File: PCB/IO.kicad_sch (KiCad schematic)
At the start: 26 parts, among them J501 Conn_02x03_Counter_Clockwise, J502 USB_C_Receptacle_USB2.0_16P, J503 Screw_Terminal_01x06, J504 Screw_Terminal_01x04, J505 Conn_01x04, J506 Conn_02x03_Counter_Clockwise, J507 Conn_01x05, Q501 NPN

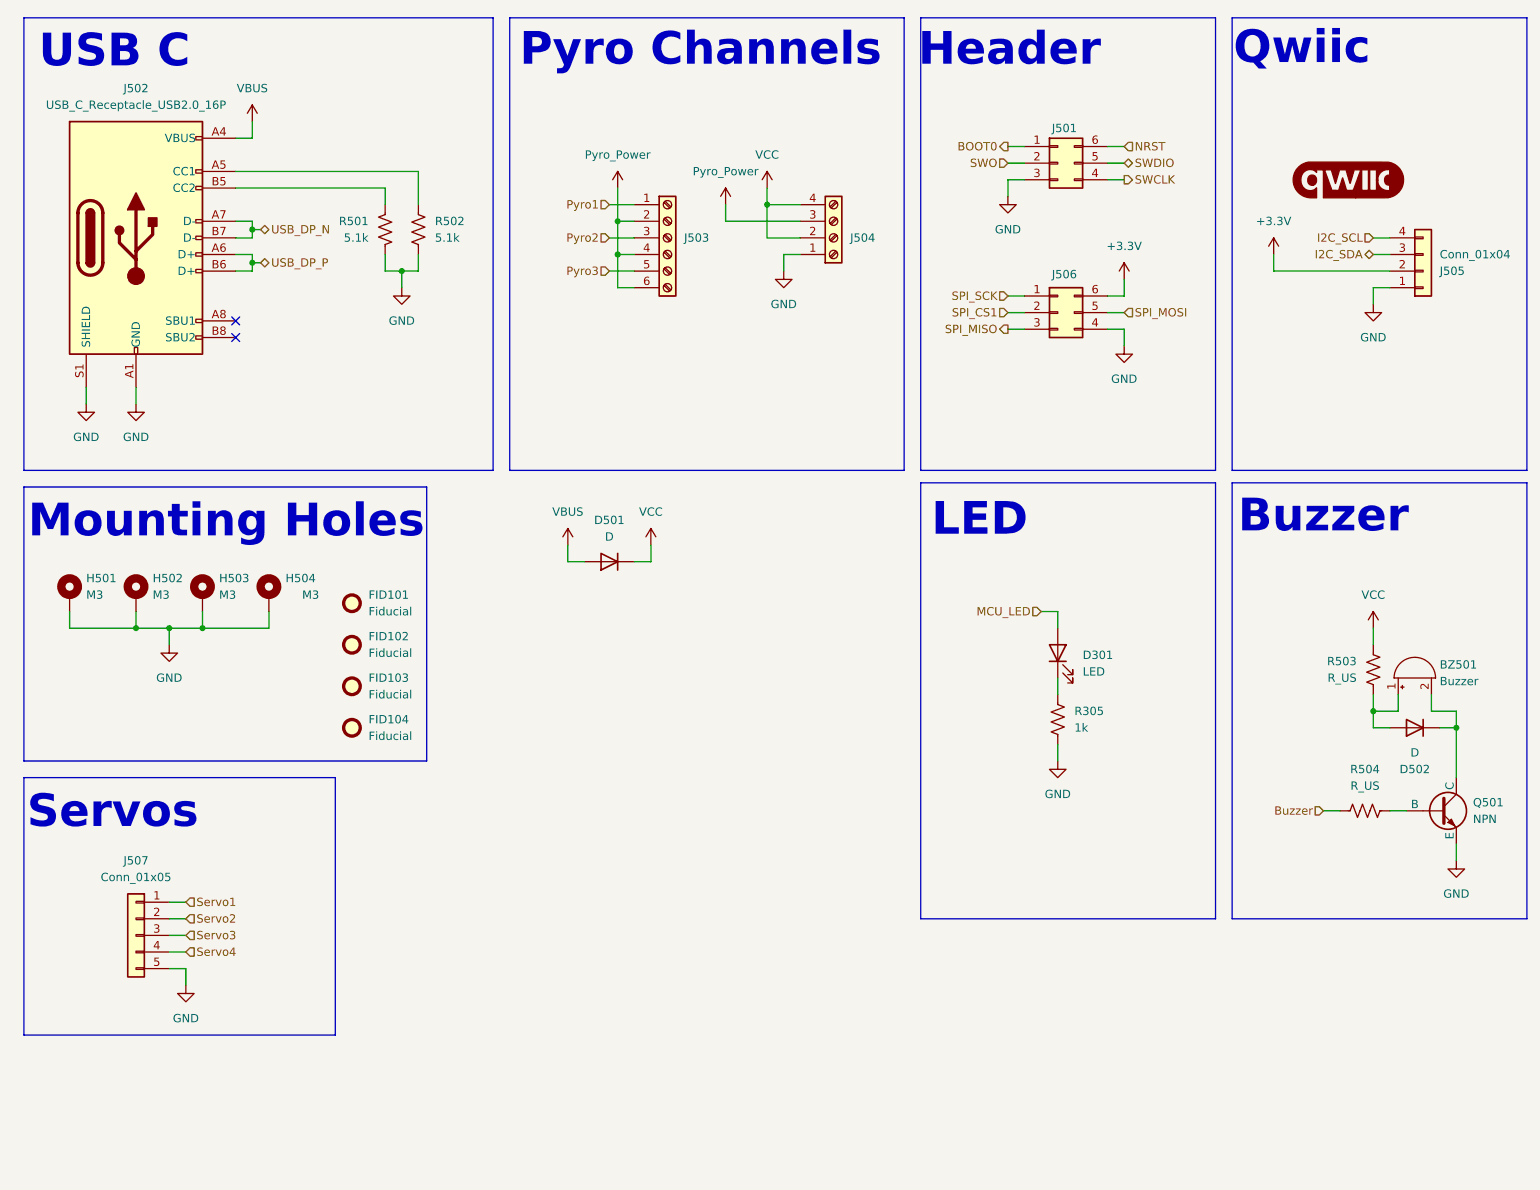
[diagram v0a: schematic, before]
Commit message: Added buzzer Added 2 more leds to MCU Fixed servo connector GND hole shape Added Servo VCC pin Added additional silkscreen for debug connections Added copper plane text "V1.1" Made 915MHz radio trace 50 Ohm
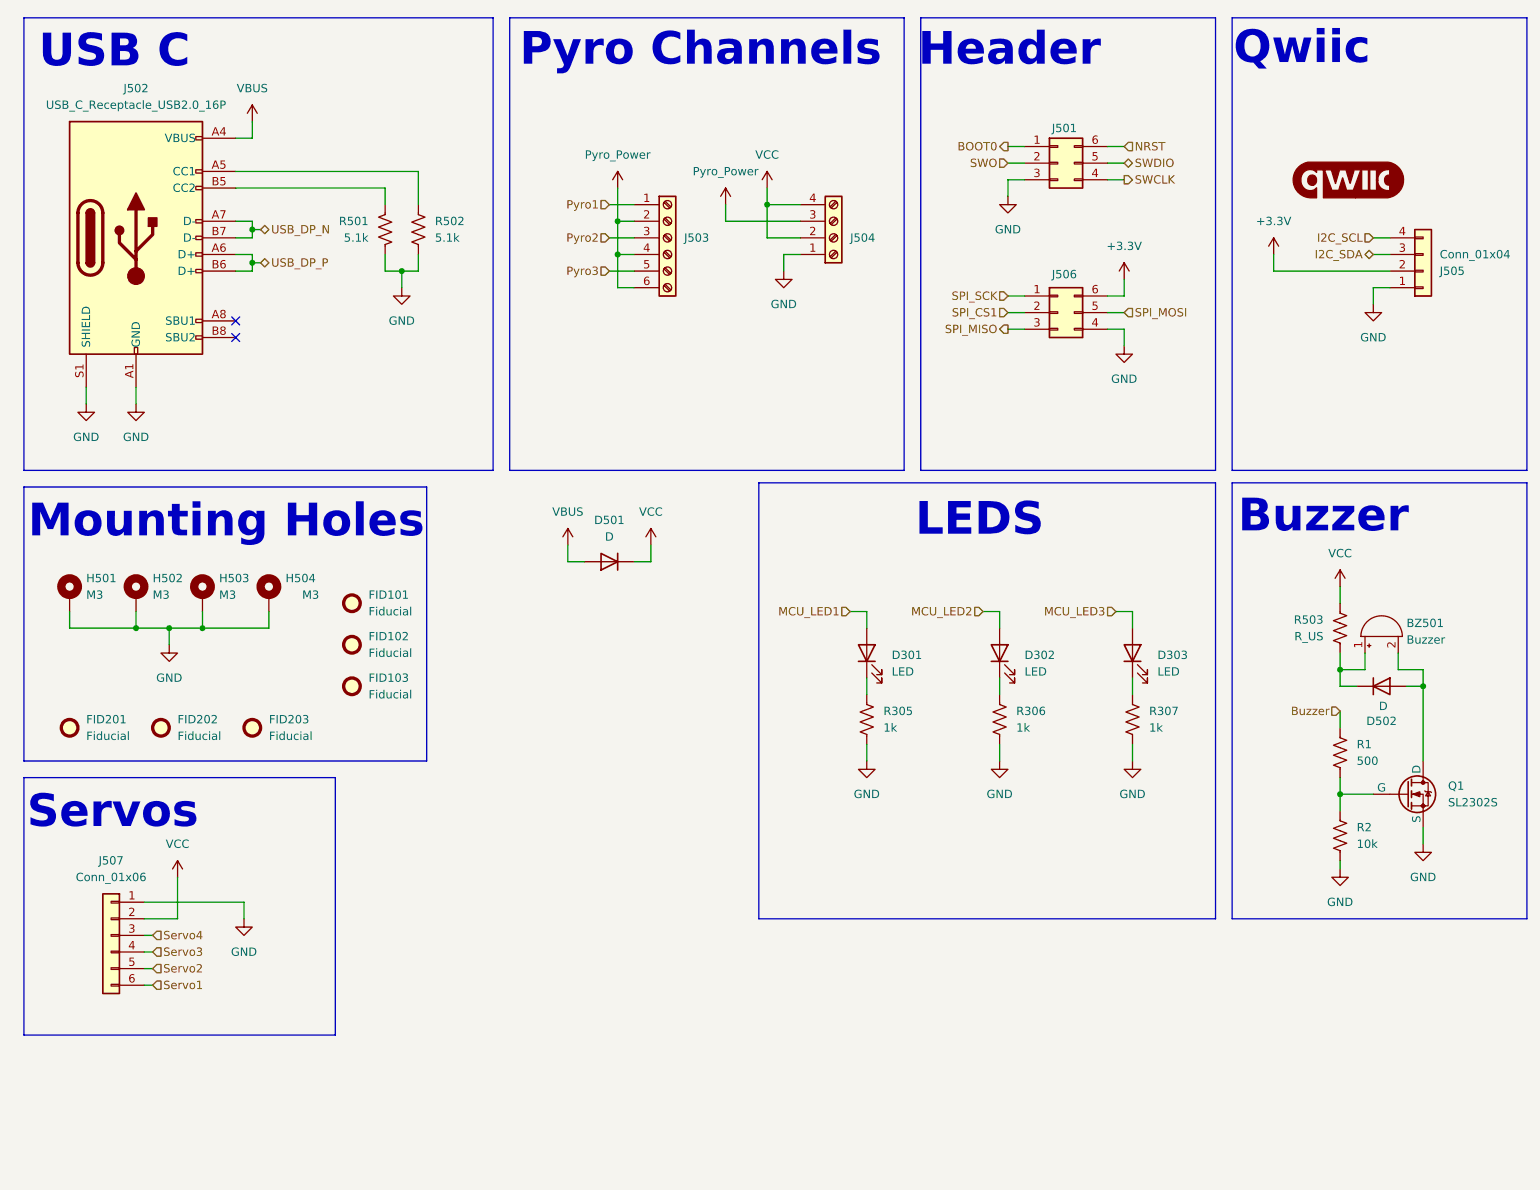
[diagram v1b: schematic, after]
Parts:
- removed Q501: NPN, symbol Simulation_SPICE:NPN
- removed R504: R_US, symbol Device:R_US
- added D301, D303: LED, LED_SMD:LED_0603_1608Metric_Pad1.05x0.95mm_HandSolder, symbol Device:LED
- added FID202, FID203: Fiducial, Fiducial:Fiducial_0.75mm_Mask1.5mm, symbol Mechanical:Fiducial
- added Q1: SL2302S, Package_TO_SOT_SMD:SOT-23-3, symbol Simulation_SPICE:NMOS
- added R1: 500, Resistor_SMD:R_0603_1608Metric_Pad0.98x0.95mm_HandSolder, symbol Device:R_US
- added R2: 10k, Resistor_SMD:R_0603_1608Metric_Pad0.98x0.95mm_HandSolder, symbol Device:R_US
- added R305, R307: 1k, Resistor_SMD:R_0603_1608Metric_Pad0.98x0.95mm_HandSolder, symbol Device:R_US
- BZ501: footprint (none) -> Buzzer:Buzzer_3mm
- D502: footprint (none) -> Package_TO_SOT_SMD:SOT-23
- J507: value Conn_01x05 -> Conn_01x06; footprint Connector_PinHeader_2.54mm:PinHeader_1x05_P2.54mm_Vertical -> Connector_PinHeader_2.54mm:PinHeader_1x06_P2.54mm_Vertical; symbol Connector_Generic:Conn_01x05 -> Connector_Generic:Conn_01x06; now in the parts list
- R503: footprint (none) -> Resistor_SMD:R_0603_1608Metric_Pad0.98x0.95mm_HandSolder
- renumbered D301 to D302, FID104 to FID201, R305 to R306
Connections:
- net Buzzer: now also R1.1
- net GND: now also J507.1 (Pin_1), Q1.2 (S), R2.2, R305.1, R307.1; no longer J507.5 (Pin_5)
- net Servo1: now also J507.6 (Pin_6); no longer J507.1 (Pin_1)
- net Servo2: now also J507.5 (Pin_5); no longer J507.2 (Pin_2)
- net Servo3: now also J507.4 (Pin_4); no longer J507.3 (Pin_3)
- net Servo4: now also J507.3 (Pin_3); no longer J507.4 (Pin_4)
- net VCC: now also J507.2 (Pin_2)
- net at BZ501.1 (+), R503.2: now also D502.1 (K); no longer D502.2 (A)
- net at BZ501.2 (-): now also D502.2 (A), Q1.3 (D); no longer D502.1 (K)
- net MCU_LED renamed MCU_LED2
- new net: Q1.1 (G), R1.2, R2.1
- new net: D301.1 (K), R305.2
- new net: D303.1 (K), R307.2
- new net MCU_LED1: D301.2 (A)
- new net MCU_LED3: D303.2 (A)
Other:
- note added: "LEDS"
- note removed: "LED"
- moved on the sheet: BZ501, D302, D502, FID201, R306, R503

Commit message: Fixed some mistakes
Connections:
- net +3.3V: now also R503.1
- net VCC: no longer R503.1
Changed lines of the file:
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@@
+	)
+	(symbol
+		(lib_id "power:+3.3V")
+		(at 215.9 101.6 0)
+		(mirror y)
+		(unit 1)
+		(exclude_from_sim no)
+		(in_bom yes)
+		(on_board yes)
+		(dnp no)
+		(fields_autoplaced yes)
+		(property "Reference" "#PWR06"
+			(at 215.9 105.41 0)
+			(effects
+				(font
+					(size 1.27 1.27)
+				)
+				(hide yes)
+			)
+		)
+		(property "Value" "+3.3V"
+			(at 215.9 96.52 0)
+			(effects
+				(font
+					(size 1.27 1.27)
+				)
+			)
+		)
+		(property "Footprint" ""
+			(at 215.9 101.6 0)
+			(effects
+				(font
+					(size 1.27 1.27)
+				)
+				(hide yes)
+			)
+		)
+		(property "Datasheet" ""
+			(at 215.9 101.6 0)
+			(effects
+				(font
+					(size 1.27 1.27)
+				)
+				(hide yes)
+			)
+		)
+		(property "Description" "Power symbol creates a global label with name \"+3.3V\""
+			(at 215.9 101.6 0)
+			(effects
+				(font
+					(size 1.27 1.27)
+				)
+				(hide yes)
+			)
+		)
+		(pin "1"
+		)
+		(instances
+			(project "Flight Computer"
+				(path "/4254ccd1-49f4-4fe6-9bf7-ccb200d73af4/0a0b3d01-7422-42e0-b725-ff9e85b891ec"
+					(reference "#PWR06")
+					(unit 1)
+				)
+			)
+		)
 	)
 	(symbol
@@
 					(unit 1)
 				)
-			)
-		)
-	)
-	(symbol
-		(lib_id "power:VCC")
-		(at 215.9 101.6 0)
-		(mirror y)
-		(unit 1)
-		(exclude_from_sim no)
-		(in_bom yes)
-		(on_board yes)
-		(dnp no)
-		(fields_autoplaced yes)
-		(property "Reference" "#PWR0517"
-			(at 215.9 105.41 0)
-			(effects
-				(font
-					(size 1.27 1.27)
-				)
-				(hide yes)
-			)
-		)
-		(property "Value" "VCC"
-			(at 215.9 96.52 0)
-			(effects
-				(font
-					(size 1.27 1.27)
-				)
-			)
-		)
-		(property "Footprint" ""
-			(at 215.9 101.6 0)
-			(effects
-				(font
-					(size 1.27 1.27)
-				)
-				(hide yes)
-			)
-		)
-		(property "Datasheet" ""
-			(at 215.9 101.6 0)
-			(effects
-				(font
-					(size 1.27 1.27)
-				)
-				(hide yes)
-			)
-		)
-		(property "Description" "Power symbol creates a global label with name \"VCC\""
-			(at 215.9 101.6 0)
-			(effects
-				(font
-					(size 1.27 1.27)
-				)
-				(hide yes)
-			)
-		)
-		(pin "1"
-		)
-		(instances
-			(project "Flight Computer"
-				(path "/4254ccd1-49f4-4fe6-9bf7-ccb200d73af4/0a0b3d01-7422-42e0-b725-ff9e85b891ec"
-					(reference "#PWR0517")
-					(unit 1)
-				)

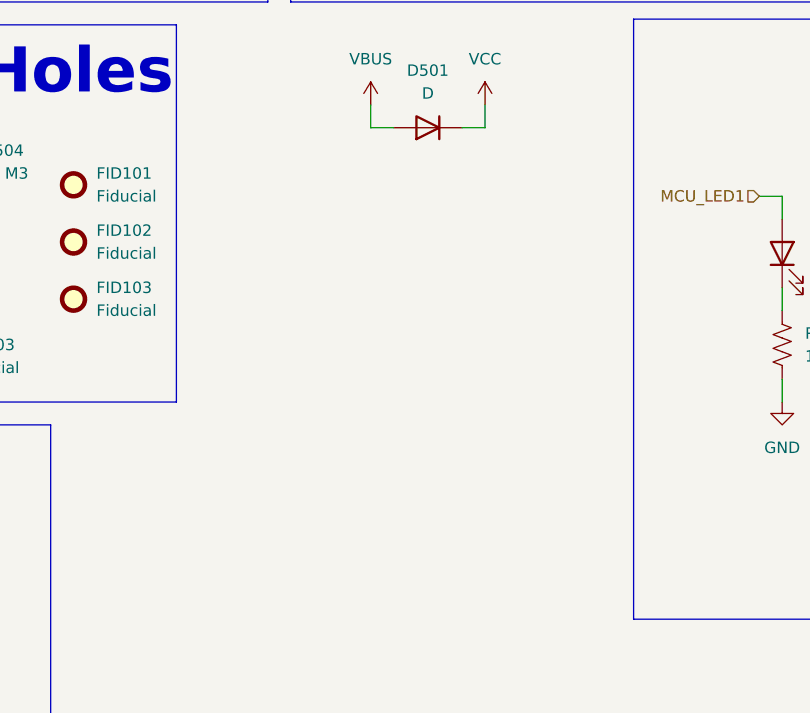
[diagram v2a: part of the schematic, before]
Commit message: Moved compass away from power traces, minor routing changes
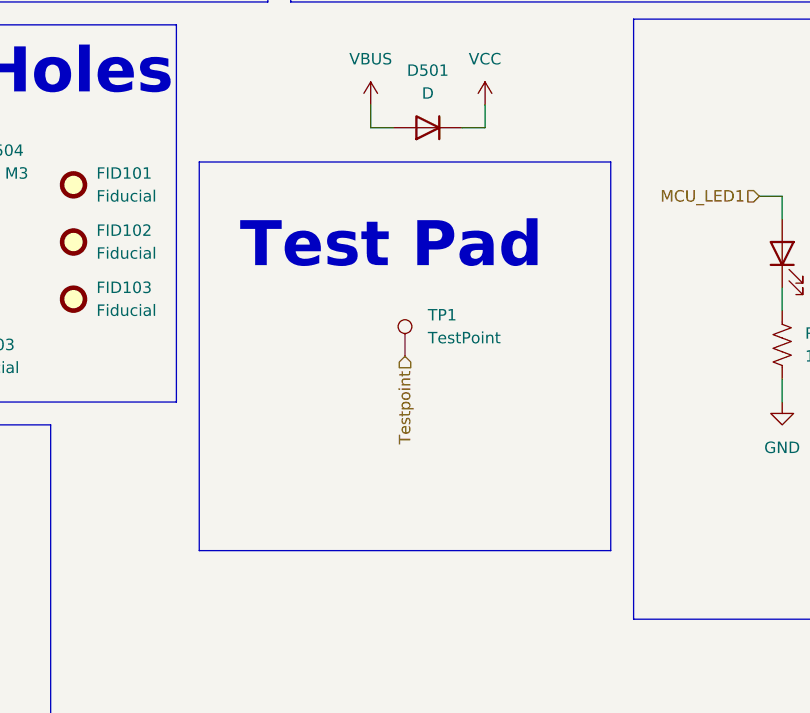
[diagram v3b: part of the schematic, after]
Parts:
- added TP1: TestPoint, symbol Connector:TestPoint
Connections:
- new net Testpoint: TP1.1
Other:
- note added: "Test Pad"
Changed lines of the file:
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@@
 	)
 	(rectangle
+		(start 78.74 101.6)
+		(end 124.46 144.78)
+		(stroke
+			(width 0)
+			(type default)
+		)
+		(fill
+			(type none)
+		)
+	)
+	(rectangle
 		(start 127 85.725)
 		(end 196.85 152.4)
@@
 		)
 	)
+	(text "Test Pad"
+		(exclude_from_sim no)
+		(at 100.076 110.998 0)
+		(effects
+			(font
+				(size 5 5)
+				(thickness 1)
+				(bold yes)
+			)
+		)
+	)
 	(text "Pyro Channels"
 		(exclude_from_sim no)
@@
 		)
 	)
+	(hierarchical_label "Testpoint"
+		(shape input)
+		(at 101.6 123.19 270)
+		(effects
+			(font
+				(size 1.27 1.27)
+			)
+			(justify right)
+		)
+	)
 	(hierarchical_label "Servo3"
 		(shape input)
@@
 					(unit 1)
 				)
+			)
+		)
+	)
+	(symbol
+		(lib_id "Connector:TestPoint")
+		(at 101.6 123.19 0)
+		(unit 1)
+		(exclude_from_sim no)
+		(in_bom yes)
+		(on_board yes)
+		(dnp no)
+		(fields_autoplaced yes)
+		(property "Reference" "TP1"
+			(at 104.14 118.6179 0)
+			(effects
+				(font
+					(size 1.27 1.27)
+				)
+				(justify left)
+			)
+		)
+		(property "Value" "TestPoint"
+			(at 104.14 121.1579 0)
+			(effects
+				(font
+					(size 1.27 1.27)
+				)
+				(justify left)
+			)
+		)
+		(property "Footprint" ""
+			(at 106.68 123.19 0)
+			(effects
+				(font
+					(size 1.27 1.27)
+				)
+				(hide yes)
+			)
+		)
+		(property "Datasheet" "~"
+			(at 106.68 123.19 0)
+			(effects
+				(font
+					(size 1.27 1.27)
+				)
+				(hide yes)
+			)
+		)
+		(property "Description" "test point"
+			(at 101.6 123.19 0)
+			(effects
+				(font
+					(size 1.27 1.27)
+				)
+				(hide yes)
+			)
+		)
+		(pin "1"
+		)
+		(instances
+			(project ""
+				(path "/4254ccd1-49f4-4fe6-9bf7-ccb200d73af4/0a0b3d01-7422-42e0-b725-ff9e85b891ec"
+					(reference "TP1")
+					(unit 1)
+				)

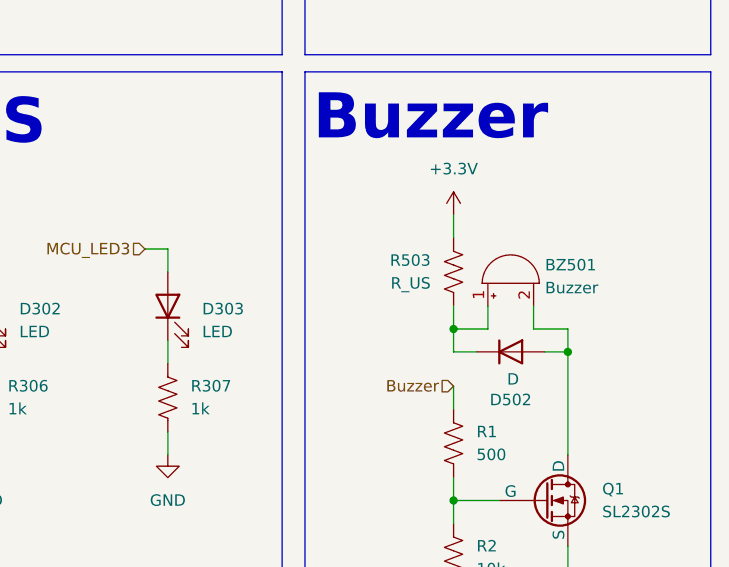
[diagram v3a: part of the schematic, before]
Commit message: added resistor value to buzzer current limiting resistor
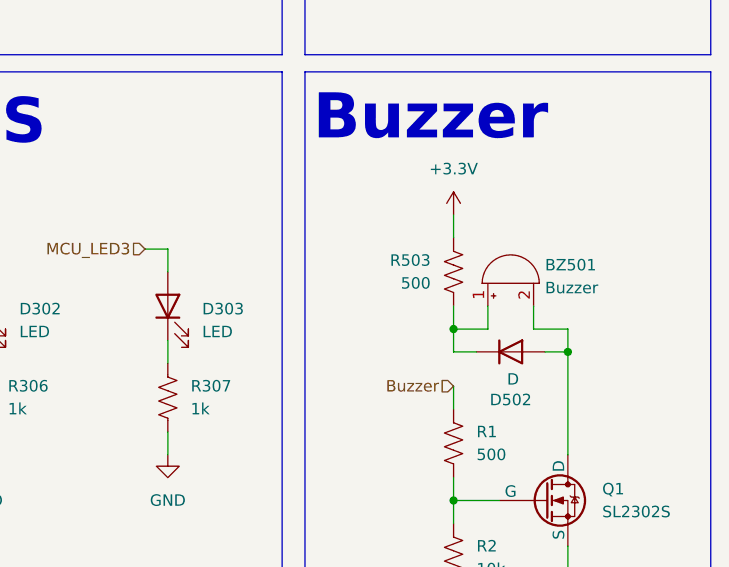
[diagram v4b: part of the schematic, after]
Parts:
- R503: value R_US -> 500
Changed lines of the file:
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@@
 			)
 		)
-		(property "Value" "R_US"
+		(property "Value" "500"
 			(at 213.36 109.2199 0)
 			(effects
